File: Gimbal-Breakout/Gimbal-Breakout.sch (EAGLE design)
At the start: 4 parts

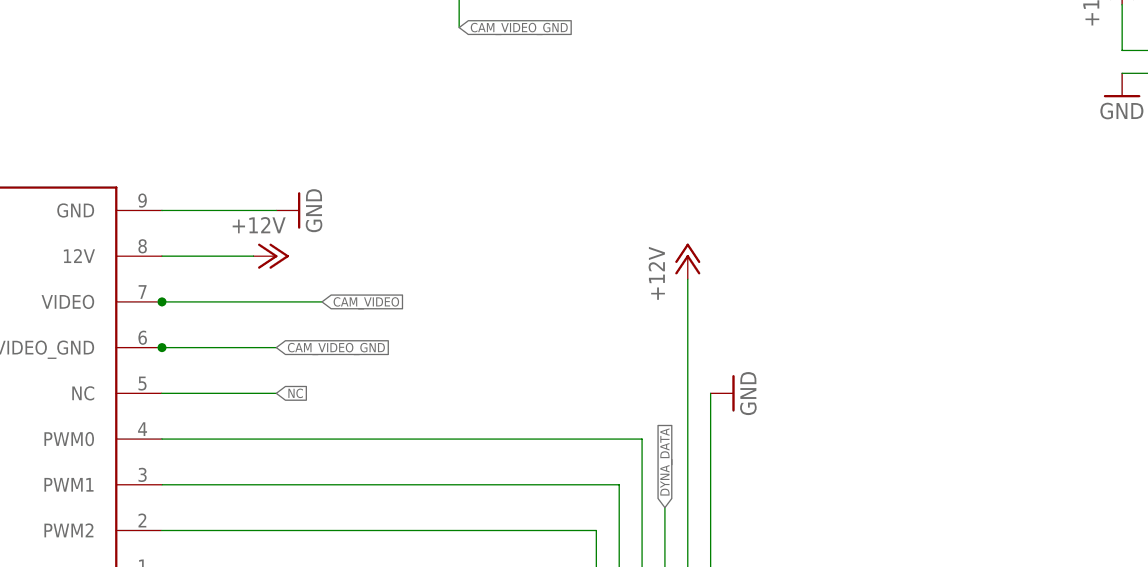
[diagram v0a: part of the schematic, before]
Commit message: finished gimbal breakout
added mounting holes
labeled board
fixed traces
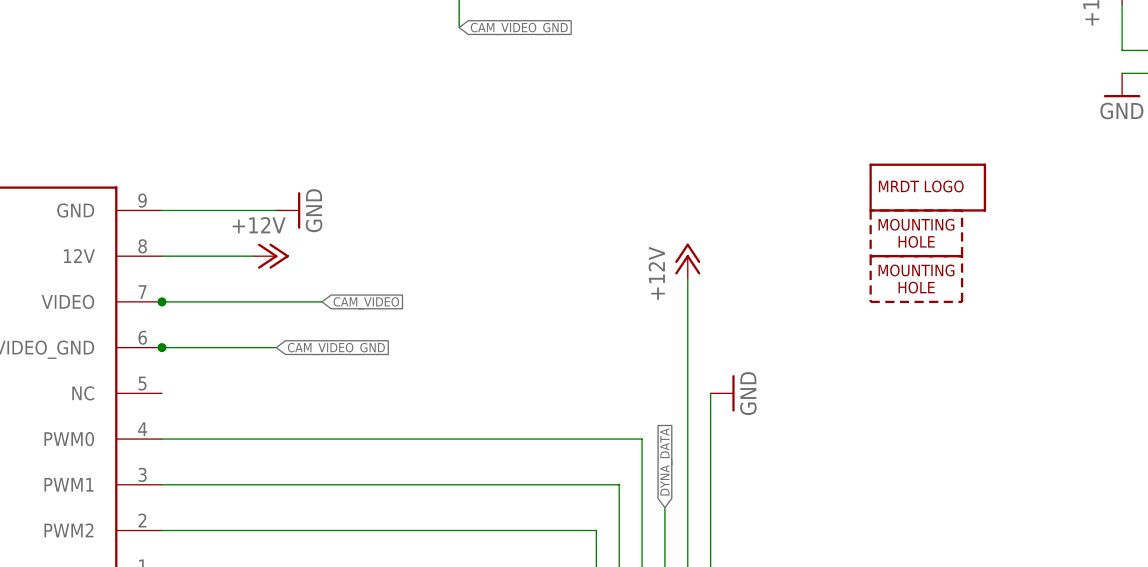
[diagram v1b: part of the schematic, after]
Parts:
- added H1, H2: MOUNTING_HOLE#4, MRDT-Hardware:MOUNTING_HOLE#4
- added LOGO1: MRDT_LOGO, MRDT-Hardware:MRDT_LOGO
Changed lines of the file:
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@@
 <part name="U$3" library="MRDT-Connectors" deviceset="SL07" device="-HORIZ"/>
 <part name="U$4" library="MRDT-2015-General" deviceset="CAMERA_BREAKOUT" device=""/>
+<part name="H1" library="MRDT-Hardware" deviceset="MOUNTING_HOLE" device="#4"/>
+<part name="H2" library="MRDT-Hardware" deviceset="MOUNTING_HOLE" device="#4"/>
+<part name="LOGO1" library="MRDT-Hardware" deviceset="MRDT_LOGO" device=""/>
 </parts>
 <sheets>
@@
 <instance part="U$3" gate="G$1" x="193.04" y="233.68" rot="R180"/>
 <instance part="U$4" gate="G$1" x="109.22" y="259.08"/>
+<instance part="H1" gate="G$1" x="208.28" y="297.18"/>
+<instance part="H2" gate="G$1" x="208.28" y="292.1"/>
+<instance part="LOGO1" gate="G$1" x="208.28" y="302.26"/>
 </instances>
 <busses>
@@
 <label x="185.42" y="269.24" size="1.016" layer="95" rot="R90" xref="yes"/>
 <pinref part="U$3" gate="G$1" pin="3"/>
-</segment>
-</net>
-<net name="NC" class="0">
-<segment>
-<wire x1="129.54" y1="281.94" x2="142.24" y2="281.94" width="0.1524" layer="91"/>
-<label x="142.24" y="281.94" size="1.016" layer="95" xref="yes"/>
 </segment>
 </net>
@@
 </schematic>
 </drawing>
+<compatibility>
+<note version="6.3" minversion="6.2.2" severity="warning">
+Since Version 6.2.2 text objects can contain more than one line,
+which will not be processed correctly with this version.
+</note>
+</compatibility>
 </eagle>
